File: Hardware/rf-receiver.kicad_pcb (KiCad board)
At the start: 4 copper layers, 97 x 50 mm, 156 parts, among them CON1 FPC_6POS, IC1 ATSAMD21G18A-AU, IC2 AD9954, IC3 74LVC74, J2 Conn_Coaxial, J6 AudioJack3_Ground, P1 ROT_ENC, SW1 BTN1, SW2 BTN2, SW3 BTN3, U1 74HC14, U10 TPS62173DSG, U11 MIC5504-1.8YM5, U12 MIC5504-1.8YM5, U2 RC1602A, U3 TXB0108PWR, U4 MIC5504-3.3YM5, U5 OPA300, U7 Transformer, U8 NE5532, U9 74CBTLV3253, Y1 Crystal_Small

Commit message: Moved IQ out to the back
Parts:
- moved J6 41.7 mm to (124.8, 53.1), turned to 270 degrees
- moved C61 25.8 mm to (135.4, 63.0)
- moved C62 25.8 mm to (135.4, 61.7)
- moved C64 25.8 mm to (135.4, 59.2)
- moved C65 25.8 mm to (135.4, 58.0)
- moved R29 25.8 mm to (135.4, 60.5)
- moved R30 25.8 mm to (135.4, 64.2)
- moved U8 25.8 mm to (128.4, 62.2)
- moved C73 25.8 mm to (122.0, 60.5)
- moved C74 25.8 mm to (122.0, 59.2)
- moved R31 25.8 mm to (122.0, 61.7)
- moved R32 25.8 mm to (122.0, 58.0)
- moved SW2 12.1 mm to (145.8, 94.7), turned to 270 degrees
- moved C45 10.7 mm to (139.7, 63.2)
- moved C46 10.7 mm to (150.2, 66.5)
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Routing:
- net +12V: track 82.6 -> 56.6 mm, vias 2 -> 6
- net /Tayoe Mixer sheet/270_deg: track 34.1 -> 55.4 mm, vias 0 -> 2
- net +3V3: track 113.1 -> 131.9 mm
- net /Tayoe Mixer sheet/90_deg: track 28.5 -> 43.1 mm, vias 6 -> 3
- net /AD9954sheet/COMP_OUT: track 31.6 -> 42.3 mm
- net Net-(C7-Pad1): track 11.0 -> 17.9 mm
- net /Tayoe Mixer sheet/RF_IN_A: track 5.83 -> 12.5 mm
- net /Tayoe Mixer sheet/180_deg: track 38.5 -> 43.3 mm
- net /Tayoe Mixer sheet/0_deg: track 33.7 -> 37.0 mm, vias 4 -> 3
- net Net-(R5-Pad2): track 5.82 -> 8.23 mm
- net Net-(R10-Pad1): track 5.91 -> 8.05 mm
- net Net-(R6-Pad2): track 5.92 -> 7.33 mm
- net Net-(C6-Pad1): track 10.1 -> 8.76 mm

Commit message: Added BOM
Added BOM.csv
Added Micro-USB
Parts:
- removed J6: AudioJack3_Ground, athir:SJ1-35235
- added J1: Conn_01x05_Female, athir:SJ1-35235, F.Cu at (125.3, 69.2)
- added J3: USB_B_Micro, Connector_USB:USB_Micro-B_Molex-105017-0001, F.Cu at (90.7, 65.7)
- added R3: R_Small, Resistor_SMD:R_0402_1005Metric, F.Cu at (87.2, 74.6)
- added R4: R_Small, Resistor_SMD:R_0402_1005Metric, F.Cu at (86.2, 74.6)
- C52, C76: footprint Capacitor_SMD:C_0402_1005Metric -> Capacitor_SMD:CP_Elec_6.3x7.7
- J2: footprint Connector_Coaxial:SMA_Molex_73251-1153_EdgeMount_Horizontal -> Connector_Coaxial:SMA_Amphenol_132289_EdgeMount
- MH1, MH2, MH3, MH4: footprint MountingHole:MountingHole_4.3mm_M4_Pad -> MountingHole:MountingHole_2.7mm_M2.5_Pad
- moved W2 22.3 mm to (70.0, 94.5)
- moved C76 18.9 mm to (95.5, 73.8), turned to 270 degrees
- moved PSU+1 18.4 mm to (98.2, 65.2)
- moved PSU-1 18.4 mm to (108.0, 65.2)
- moved FL1 18.4 mm to (103.5, 65.6)
- moved MH4 17.7 mm to (71.2, 109.0)
- moved C77 17.5 mm to (100.9, 69.0)
- moved C78 17.5 mm to (103.1, 69.0)
- moved C79 17.5 mm to (103.1, 70.2)
- moved L8 17.5 mm to (107.8, 71.2)
- moved R33 17.5 mm to (105.1, 71.0)
- moved U10 17.5 mm to (102.1, 72.8)
- moved MH3 17.5 mm to (153.8, 109.0)
- moved W1 17.5 mm to (70.0, 89.0)
- moved R27 17.3 mm to (152.5, 78.8)
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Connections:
- IC1 pad 32: /USB/VCC -> /USB_VCC
- IC1 pad 33: /USB/DM -> /USB_D-
- IC1 pad 34: /USB/DP -> /USB_D+
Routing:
- net /JTAGConn58895F8D/SWDIO: track 16.0 -> 35.0 mm
- net /USB_D+: track 0.00 -> 17.9 mm
- net /USB_D-: track 0.00 -> 17.9 mm
- net /JTAGConn58895F8D/SWCLK: track 16.4 -> 34.0 mm
- net /JTAGConn58895F8D/MCU_RESET: track 10.9 -> 27.2 mm
- net /UART_TX: track 20.2 -> 33.8 mm
- net /Tayoe Mixer sheet/I_OUT: track 8.66 -> 17.9 mm
- net Net-(J3-Pad1): track 0.00 -> 9.22 mm
- net /USB_VCC: track 0.00 -> 8.82 mm
- net /Tayoe Mixer sheet/Q_OUT: track 7.13 -> 13.0 mm
- net /Tayoe Mixer sheet/DC_BIAS: track 14.0 -> 19.6 mm
- net +12V: track 56.6 -> 53.2 mm, vias 6 -> 4
- net /UART_RX: track 9.18 -> 11.7 mm
- net +1V8: track 161.0 -> 162.2 mm, vias 10 -> 11
- net GND: vias 105 -> 107
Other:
- board size 97 x 50 mm -> 90.8 x 50 mm

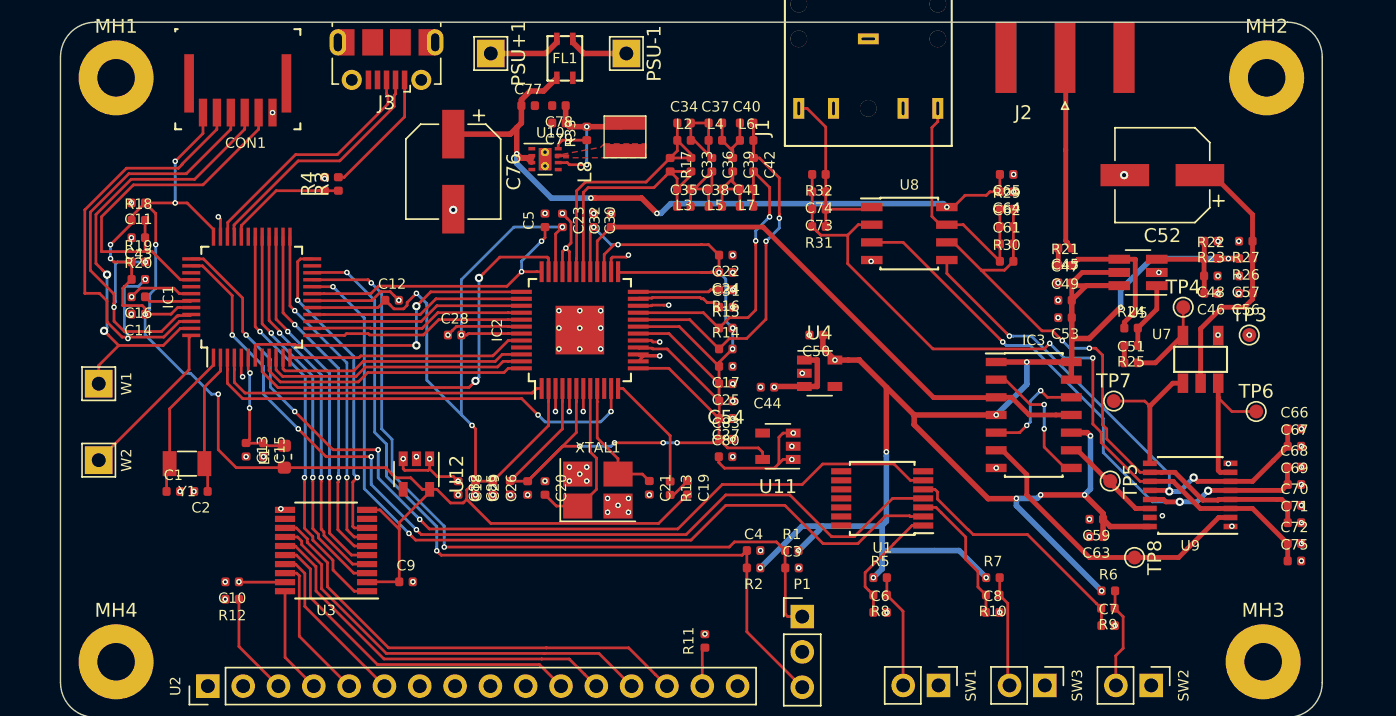
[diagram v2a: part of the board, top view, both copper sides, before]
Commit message: HW PCB changes
Added IBOM
Added extra spacing between 0402 components.
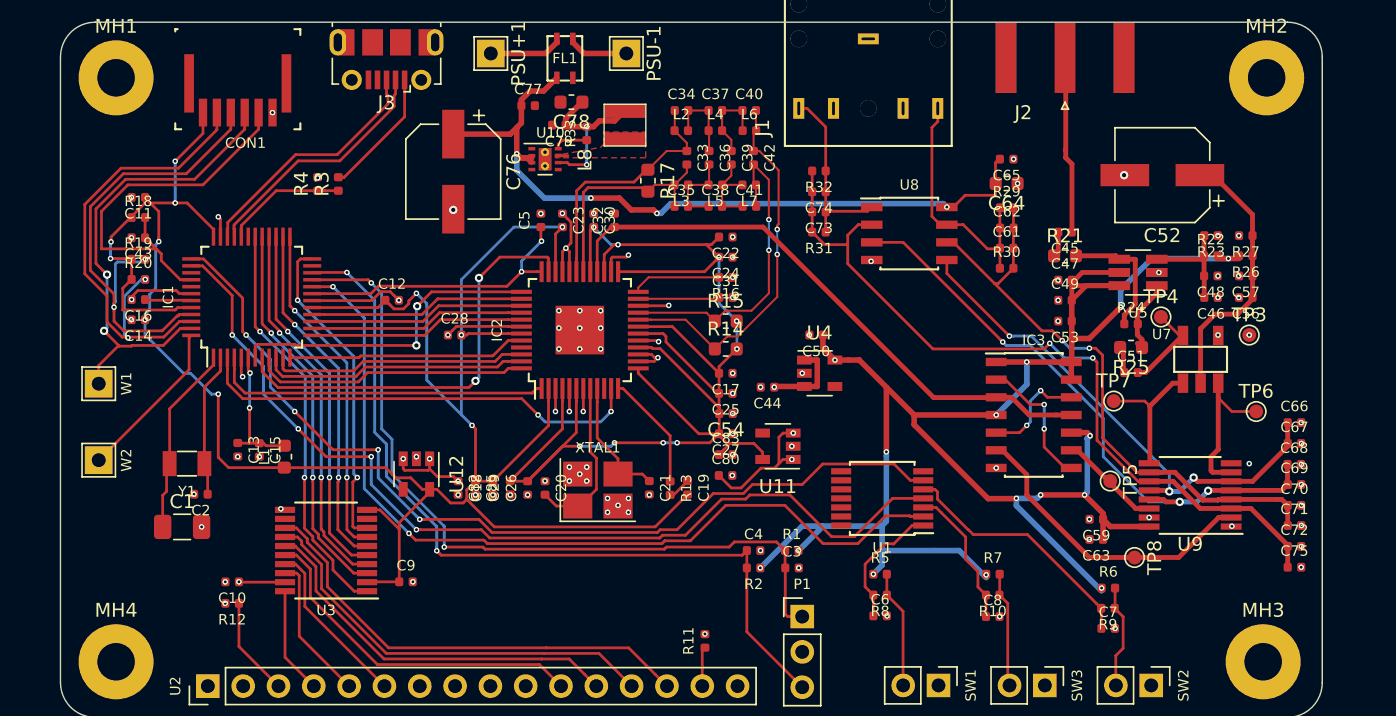
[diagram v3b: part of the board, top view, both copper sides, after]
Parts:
- C1: footprint Capacitor_SMD:C_0402_1005Metric -> Resistor_SMD:R_1206_3216Metric
- C64, C78: footprint Capacitor_SMD:C_0402_1005Metric -> Capacitor_SMD:C_0603_1608Metric
- C79: value 22uF -> 100nF
- R14, R15, R17, R21, R25: footprint Resistor_SMD:R_0402_1005Metric -> Resistor_SMD:R_0603_1608Metric
- R26, R27: value 2.2k ohm -> 2k ohm
- U9: footprint Package_SO:SSOP-16_4.4x5.2mm_P0.65mm -> Package_SO:TSSOP-16_4.4x5mm_P0.65mm
- moved C1 2.63 mm to (76.0, 99.3)
- moved R17 1.97 mm to (109.5, 74.4)
- moved TP4 1.75 mm to (146.4, 84.2)
- moved C80 1.35 mm to (115.1, 95.6)
- moved C22 1.30 mm to (115.1, 78.5)
- moved C45 1.15 mm to (139.5, 78.1)
- moved C65 1.10 mm to (135.3, 72.8)
- moved C24 1.10 mm to (115.1, 79.9)
- moved C27 1.10 mm to (115.1, 92.6)
- moved C83 1.10 mm to (115.1, 94.1)
- moved C78 0.93 mm to (104.0, 68.8)
- moved C40 0.92 mm to (116.8, 69.3)
- moved C34 0.92 mm to (111.9, 69.3)
- moved C37 0.90 mm to (114.3, 69.3)
- moved C54 0.90 mm to (115.1, 91.2)
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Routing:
- net VAA: track 103.5 -> 107.5 mm
- net Net-(C1-Pad1): track 11.0 -> 13.4 mm
- net Net-(C33-Pad2): track 18.5 -> 16.1 mm
- net +1V8: track 162.2 -> 163.8 mm
- net +5V: track 35.0 -> 36.4 mm
- net +12V: track 53.2 -> 54.6 mm
- net Net-(C34-Pad2): track 7.18 -> 5.85 mm
- net Net-(C33-Pad1): track 19.4 -> 18.1 mm
- net Net-(C35-Pad2): track 7.21 -> 5.99 mm
- net /Tayoe Mixer sheet/RF_IN_A: track 12.5 -> 11.3 mm
- net /JTAGConn58895F8D/SWDIO: track 35.0 -> 34.1 mm
- net /Tayoe Mixer sheet/270_deg: track 55.4 -> 56.2 mm
- net /Tayoe Mixer sheet/RF_B: track 10.4 -> 11.1 mm
- net Net-(R24-Pad2): track 4.87 -> 5.59 mm
- net Net-(R21-Pad2): track 10.0 -> 9.33 mm
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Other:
- rule trace_min: 0.2 -> 0.15

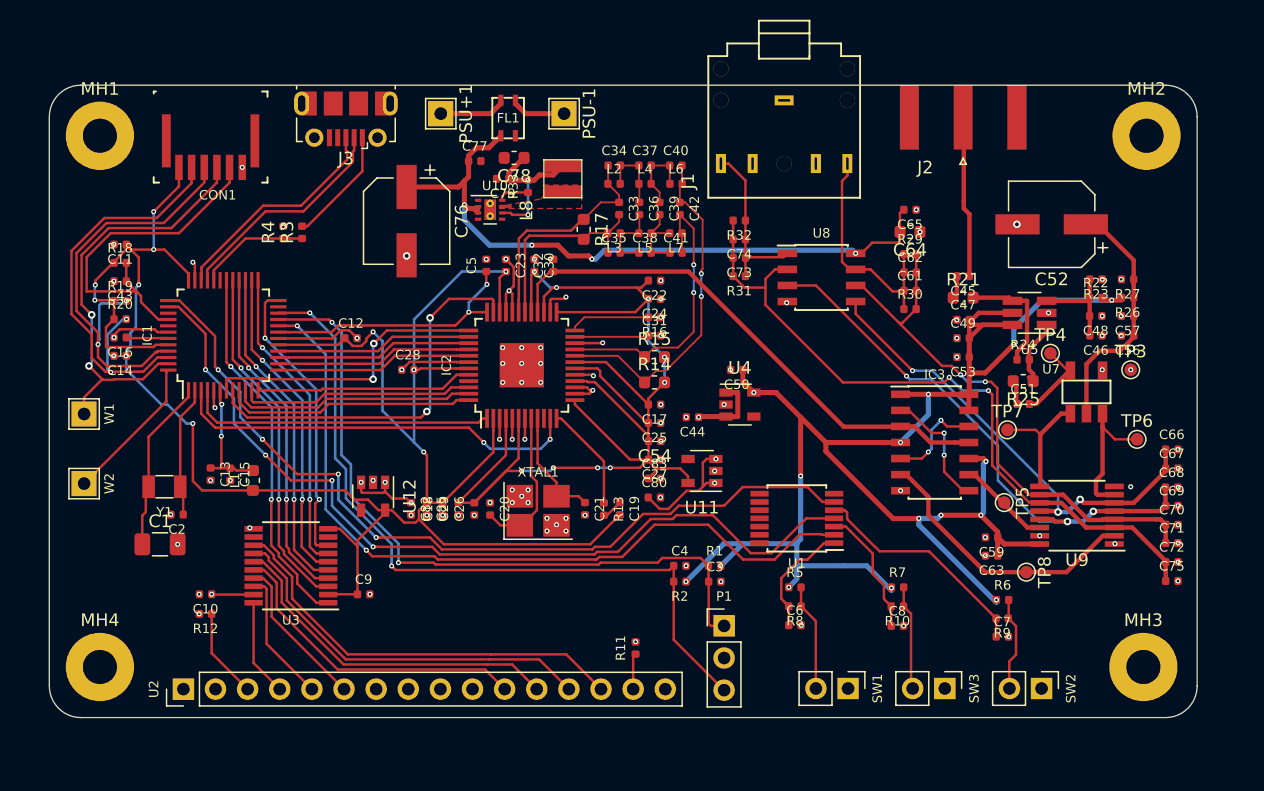
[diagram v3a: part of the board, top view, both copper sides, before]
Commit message: Fixed Silkscreen
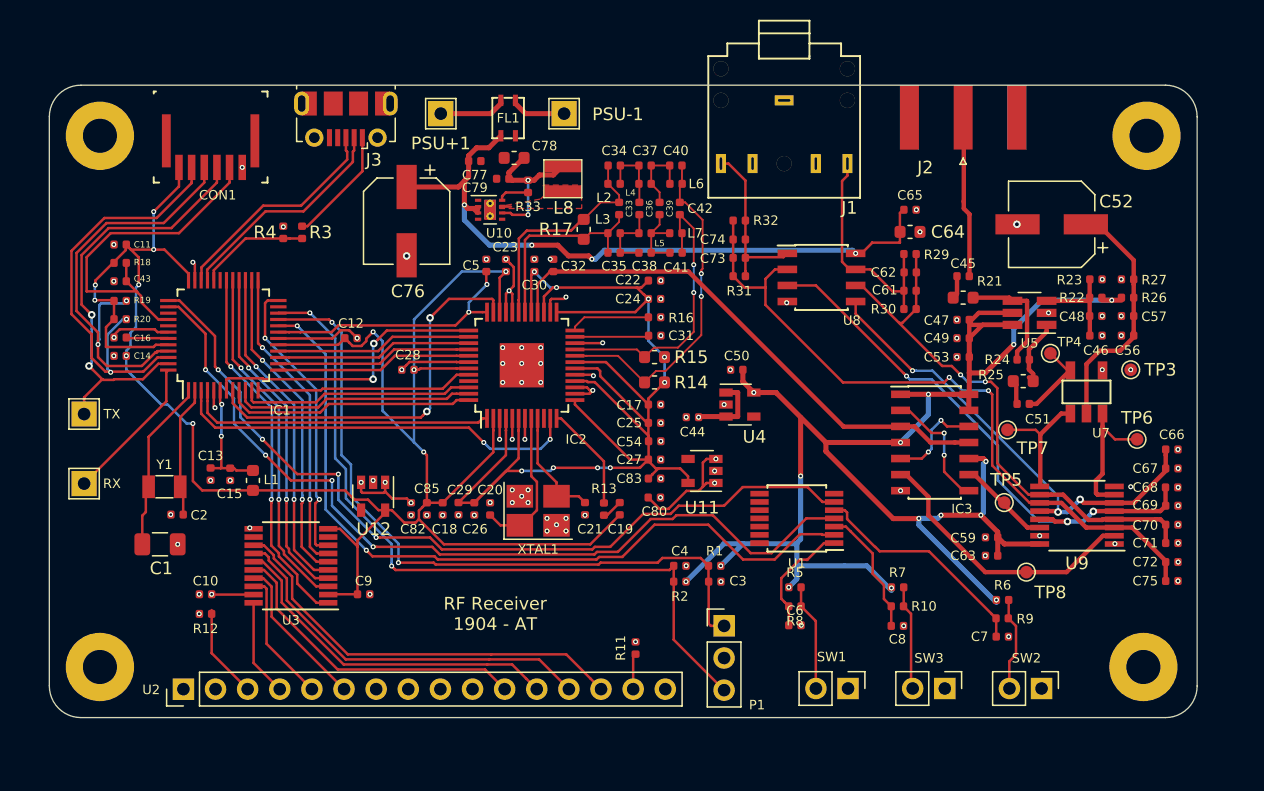
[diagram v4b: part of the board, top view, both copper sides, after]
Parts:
- renumbered W2 to RX, W1 to TX
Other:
- board text added: "RF Receiver 1904 - AT"

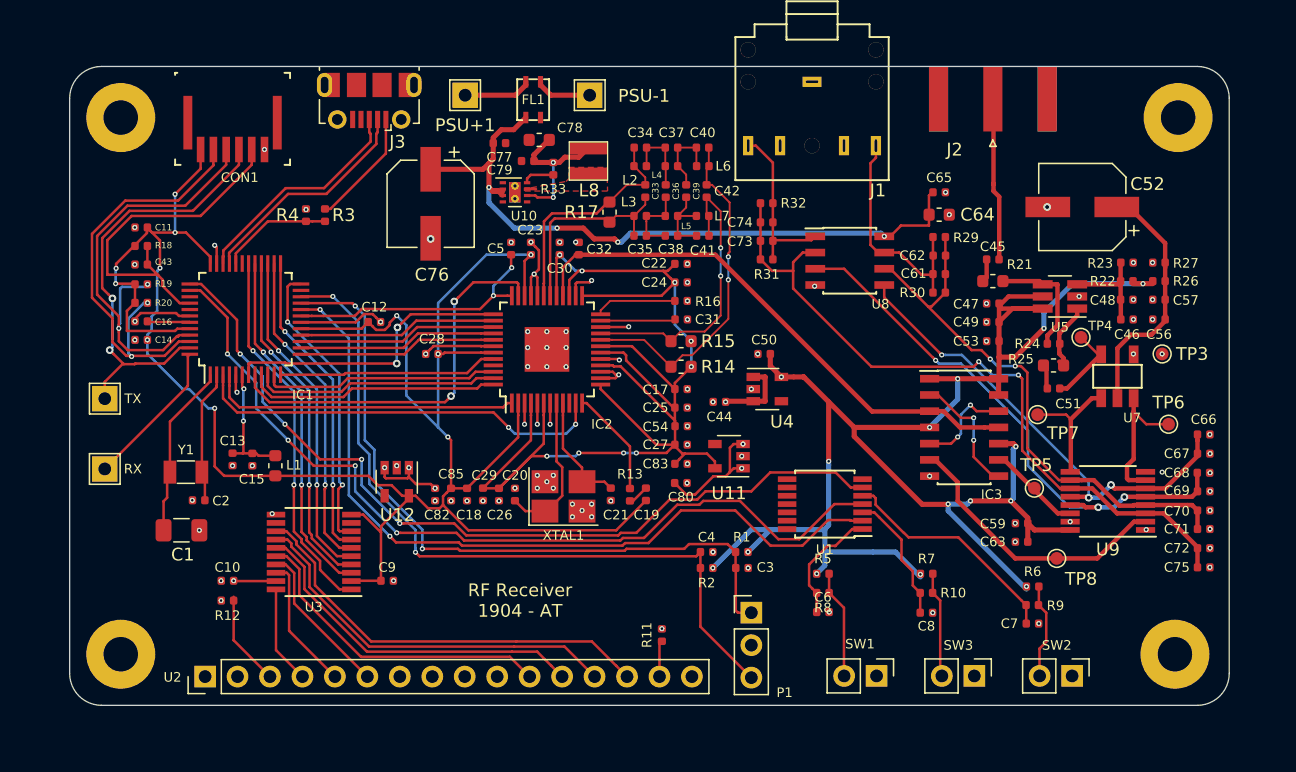
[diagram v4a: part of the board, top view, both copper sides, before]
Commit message: Added GND vias
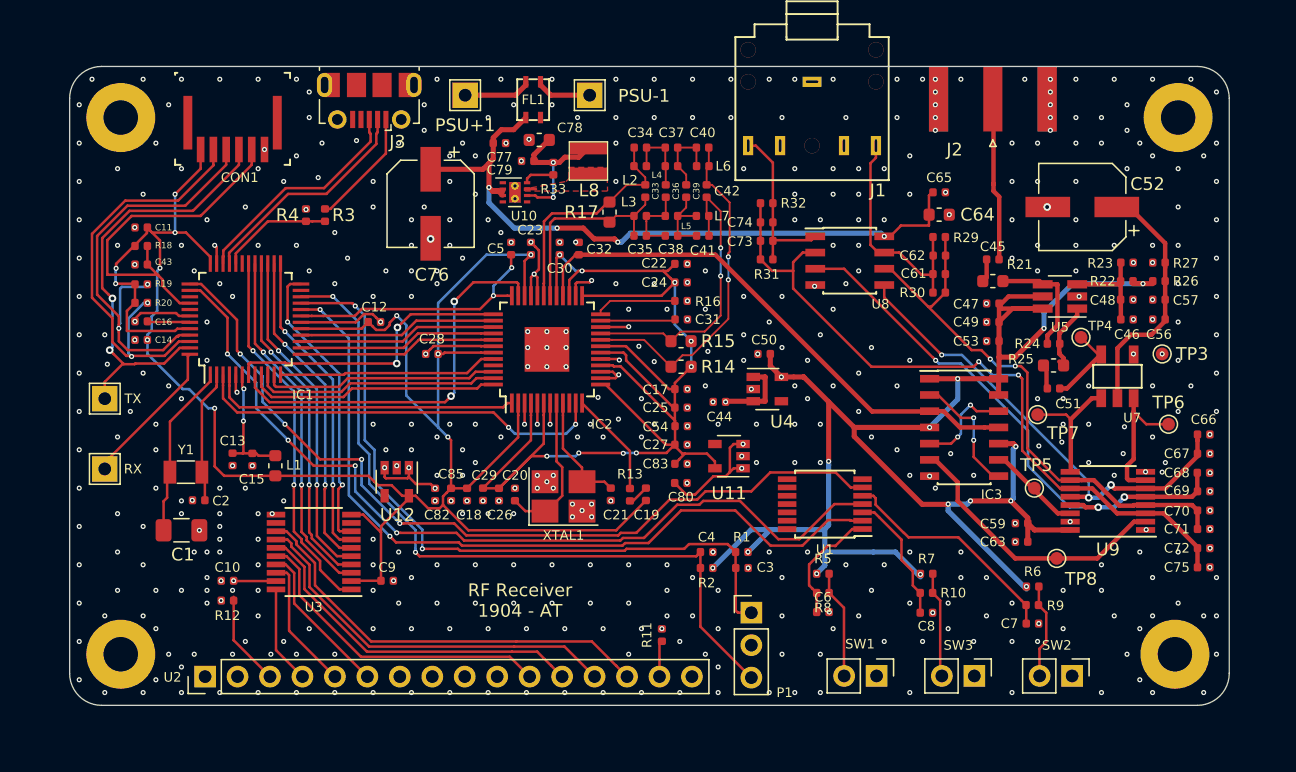
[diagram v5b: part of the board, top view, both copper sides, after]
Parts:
- added REF**: Hammond_1550B, athir:Hammond_1550B, F.Cu at (113.2, 90.0)
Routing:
- net GND: vias 107 -> 516
- net +5V: vias 10 -> 11

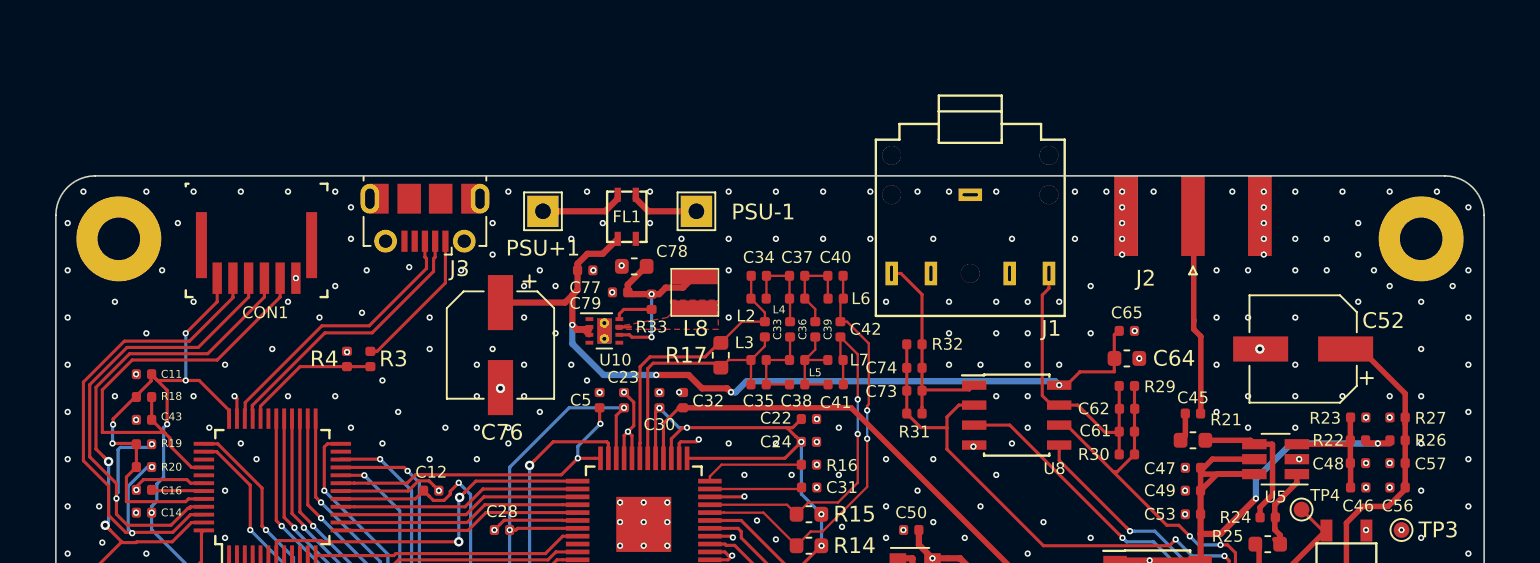
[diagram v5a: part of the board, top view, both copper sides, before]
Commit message: HW: Fixed mini-jack position
Added Gerber files.
Moved the mini-jack back and added a cutout in the PCB.
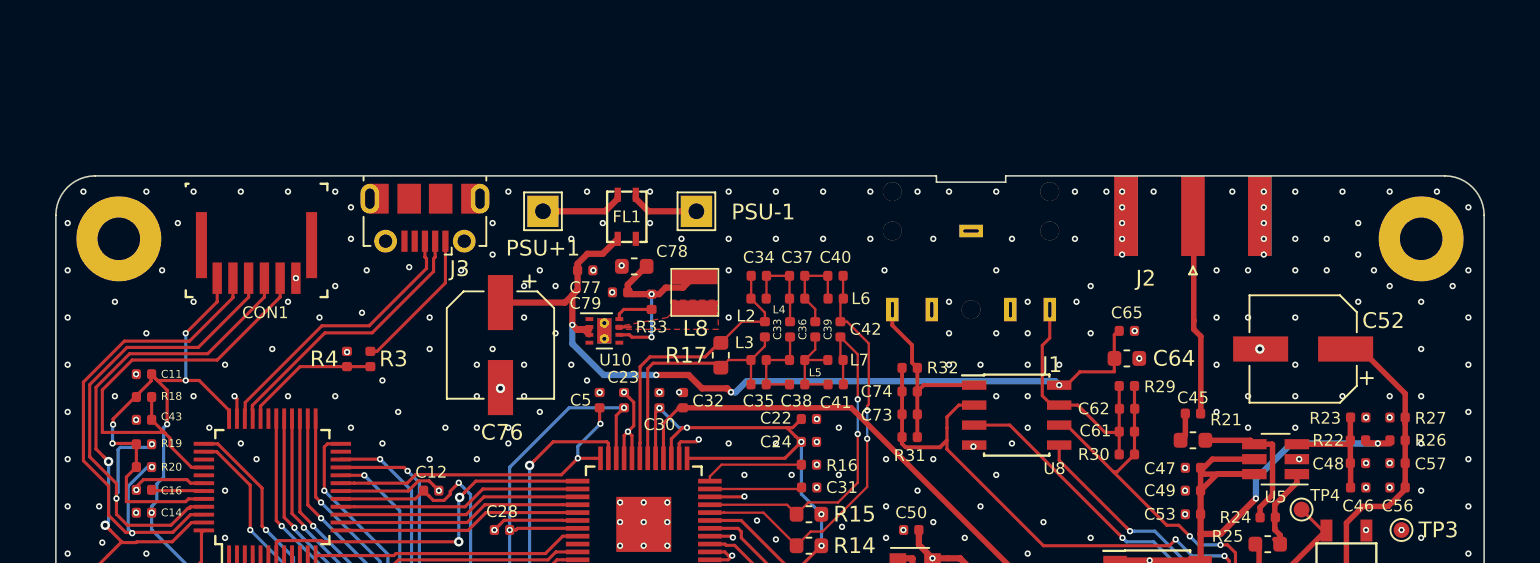
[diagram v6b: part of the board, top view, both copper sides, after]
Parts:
- moved J1 2.30 mm to (125.4, 71.5)
- moved C73 1.53 mm to (121.5, 78.2)
- moved C74 1.53 mm to (121.5, 76.7)
- moved R31 1.53 mm to (121.5, 79.6)
- moved R32 1.53 mm to (121.5, 75.2)
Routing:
- net /Tayoe Mixer sheet/I_OUT: track 18.1 -> 15.8 mm
- net /Tayoe Mixer sheet/Q_OUT: track 13.6 -> 12.5 mm
- net /Tayoe Mixer sheet/270_deg: track 56.2 -> 57.0 mm
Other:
- outline, holes or cut-outs redrawn
